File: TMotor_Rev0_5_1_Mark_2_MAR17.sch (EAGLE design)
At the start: 64 parts, among them U10 DEV-16771, U3 INA125U, U4 INA125U, U5 SN65HVD230MDREP

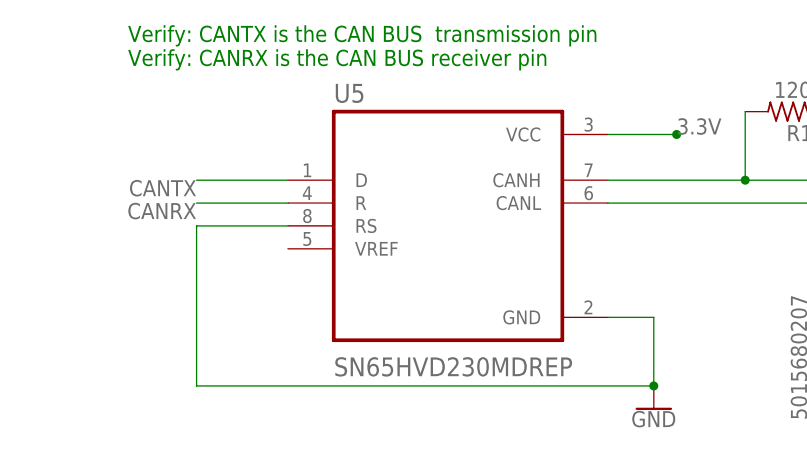
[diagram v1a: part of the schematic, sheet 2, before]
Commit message: Replaced the CAN transceiver
Replaced SN65HVD230MDREP with SN65HVD230DR
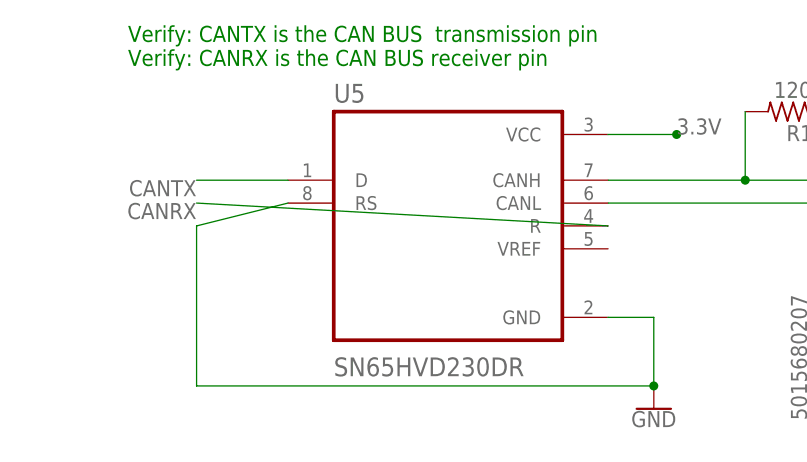
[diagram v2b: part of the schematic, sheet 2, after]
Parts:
- U5: value SN65HVD230MDREP -> SN65HVD230DR; device SnapEDA-Library:SN65HVD230MDREP -> SN65HVD230DR:SN65HVD230DR
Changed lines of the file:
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@@
 <part name="U3" library="Digikey" deviceset="INA125U" device=""/>
 <part name="U4" library="Digikey" deviceset="INA125U" device=""/>
-<part name="U5" library="SnapEDA-Library" deviceset="SN65HVD230MDREP" device=""/>
+<part name="U5" library="SN65HVD230DR" deviceset="SN65HVD230DR" device=""/>
 <part name="CAN_L0" library="SnapEDA-Library" deviceset="5015680207" device=""/>
 <part name="CAN_L1" library="SnapEDA-Library" deviceset="5015680207" device=""/>
@@
 <pinref part="GND12" gate="1" pin="GND"/>
 <pinref part="U5" gate="A" pin="RS"/>
-<wire x1="-299.72" y1="88.9" x2="-309.88" y2="88.9" width="0.1524" layer="91"/>
+<wire x1="-299.72" y1="91.44" x2="-309.88" y2="88.9" width="0.1524" layer="91"/>
 <wire x1="-309.88" y1="88.9" x2="-309.88" y2="71.12" width="0.1524" layer="91"/>
 <wire x1="-309.88" y1="71.12" x2="-259.08" y2="71.12" width="0.1524" layer="91"/>
@@
 <segment>
 <pinref part="U5" gate="A" pin="R"/>
-<wire x1="-299.72" y1="91.44" x2="-309.88" y2="91.44" width="0.1524" layer="91"/>
+<wire x1="-264.16" y1="88.9" x2="-309.88" y2="91.44" width="0.1524" layer="91"/>
 <label x="-309.88" y="91.44" size="1.778" layer="95" rot="R180"/>
 </segment>
